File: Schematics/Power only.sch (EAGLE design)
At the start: 9 parts, among them IC1 OPA548T, IC2 OPA2336P, U1 MCP4822-E/P

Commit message: added some pluggery
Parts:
- added C2, C3: 0.1µF, microbuilder:CAP_CERAMIC0805
- added J1, J2: TERMBLOCK_1X2-3.5MM, microbuilder:TERMBLOCK_1X2-3.5MM
- added JP1, JP2: (no value), microbuilder:HEADER-1X670MIL
- added R10, R11, R12, R13, R5, R6, R7, R8: 10K, microbuilder:RESISTOR0805
- added R14, R9: 0.1/1% (PT2512FK-070R1L), microbuilder:RESISTOR2512
- added SJ1, SJ2, SJ3, SJ4: (no value), microbuilder:SOLDERJUMPERREFLOW_NOPASTE
- added U2, U3: INA219BIDCNT, microbuilder:INA219
- added X1: (no value), con-phoenix-254:MPT2
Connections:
- removed net VCELL: IC1.OUT, R1.2
- new net GND: C2.2, C3.2, JP1.2, JP2.2, R10.1, R11.1, R5.1, R6.1, U2.GND, U3.GND
- new net N$10: R10.2, SJ3.2, U3.A0
- new net N$5: R6.2, SJ2.2, U2.A1
- new net N$7: R5.2, SJ1.2, U2.A0
- new net N$9: R11.2, SJ4.2, U3.A1
- new net SCL: JP1.3, JP2.3, R12.1, R7.1, U2.SCL, U3.SCL
- new net SDA: JP1.4, JP2.4, R13.1, R8.1, U2.SDA, U3.SDA
- new net VIN+: IC1.OUT, J1.2, J2.2, JP1.6, JP2.6, R1.2, R14.2, R9.2, U2.VIN+, U3.VIN+
- new net VIN-: J1.1, J2.1, JP1.5, JP2.5, R14.1, R9.1, U2.VIN-, U3.VIN-, X1-1.1, X1-2.1
- net VCC: now also C2.1, C3.1, JP1.1, JP2.1, R12.2, R13.2, R7.2, R8.2, SJ1.1, SJ2.1, SJ3.1, SJ4.1, U2.VCC, U3.VCC

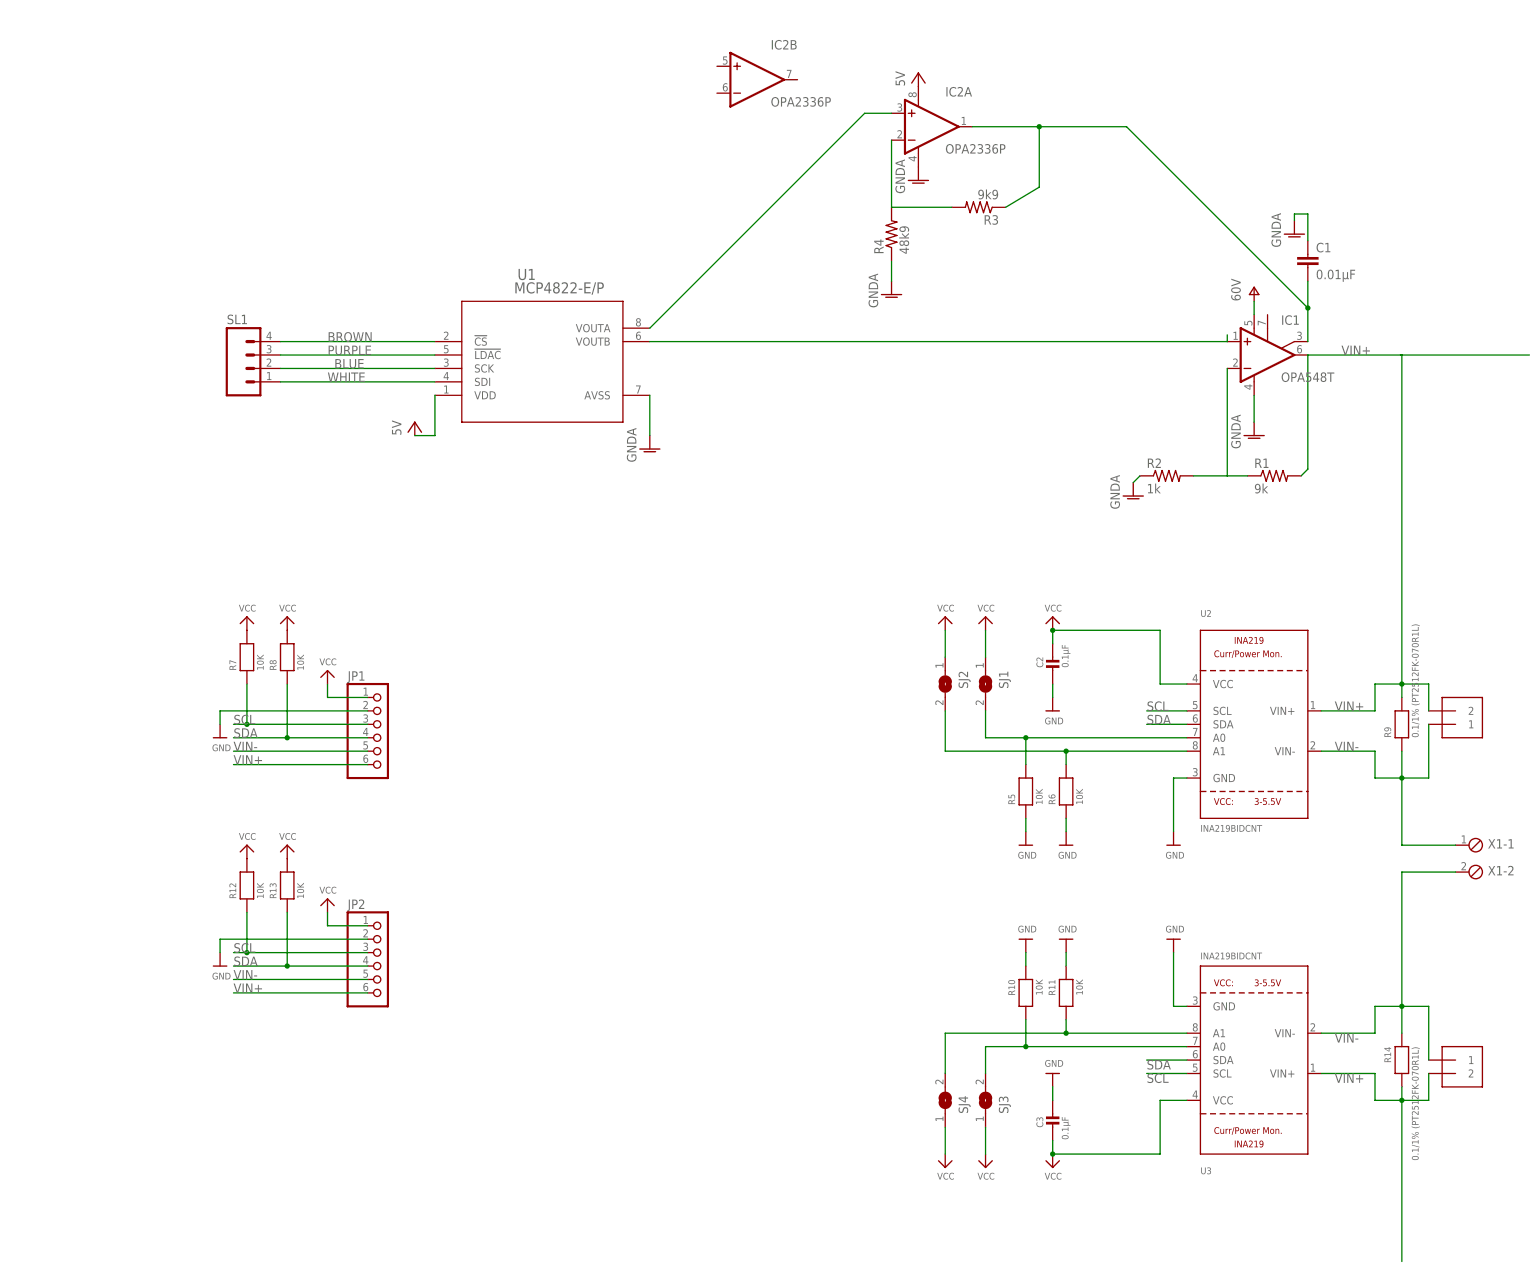
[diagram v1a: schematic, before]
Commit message: Temp sense and H bridge
plug for temp sensor wiring for H bridge to arduino
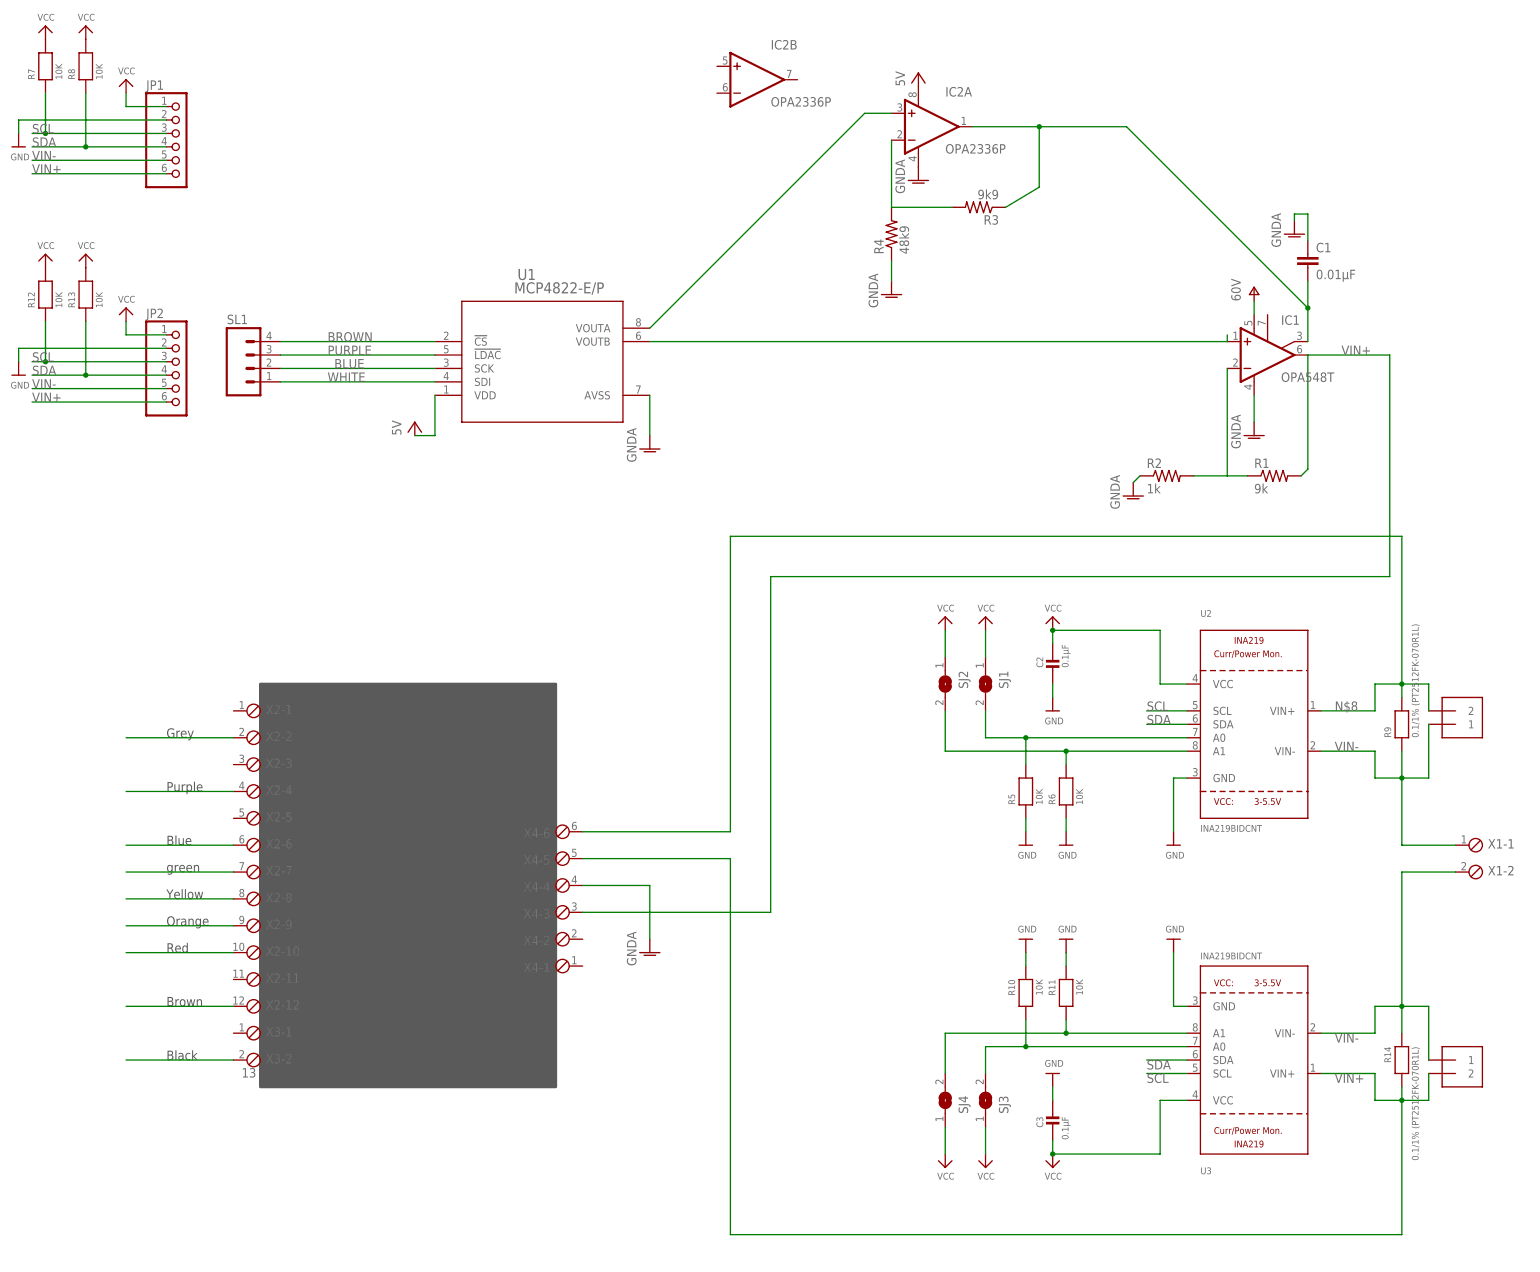
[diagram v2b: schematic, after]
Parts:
- added X2: (no value), con-phoenix-254:MPT12
- added X3: 13, con-phoenix-254:MPT2
- added X4: (no value), con-phoenix-254:MPT6
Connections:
- new net N$11: X2-2.1
- new net N$13: X2-4.1
- new net N$15: X2-6.1
- new net N$16: X2-7.1
- new net N$17: X2-8.1
- new net N$18: X2-9.1
- new net N$19: X2-10.1
- new net N$21: X2-12.1
- new net N$22: X3-2.1
- new net N$8: J1.2, R9.2, U2.VIN+, X4-6.1
- net GNDA: now also X4-4.1
- net VIN+: now also X4-3.1, X4-5.1; no longer J1.2, R9.2, U2.VIN+
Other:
- note added: "!M1FLT"
- note added: "!M1SLP"
- note added: "!M2FLT"
- note added: "!M2SLP"
- note added: "13"
- note added: "Black"
- note added: "Blue"
- note added: "Brown"
- note added: "GND"
- note added: "Grey"
- note added: "M1A"
- note added: "M1DIR"
- note added: "M1PWM"
- note added: "M2A"
- note added: "M2B"
- note added: "M2DIR"
- note added: "M2PWM"
- note added: "Orange"
- note added: "Purple"
- note added: "Red"
- note added: "VIN"
- note added: "Yellow"
- note added: "green"
- moved on the sheet: JP1, JP2, R12, R13, R7, R8
